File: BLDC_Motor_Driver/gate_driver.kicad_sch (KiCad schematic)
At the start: 23 parts, among them U1 TMC9660, U2 SN74LVC3G17

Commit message: added breakout connector and reformatted some things
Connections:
- net 1.8V_VOUT renamed 1V8_VOUT
- net 3.3V_REG renamed 3V3_REG
- no-connect marks 17 -> 0
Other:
- note removed: "TODO: map HALL_CONN_X to GPIOs"
- moved on the sheet: C10, C11, C12, C9, R1, R2, R3, R4, R5, R6, U2

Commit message: schematics more or less done
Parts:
- added C411, C413, C416: 100pF, Capacitor_SMD:C_0603_1608Metric, symbol Device:C
- added C418: 100nF, Capacitor_SMD:C_0603_1608Metric, symbol Device:C
- added D401: ORANGE_LED, LED_SMD:LED_0603_1608Metric, symbol Device:LED
- added R401, R402, R403: 10k, Resistor_SMD:R_0603_1608Metric, symbol Device:R_US
- added R404: 470, Resistor_SMD:R_0603_1608Metric, symbol Device:R_US
- added R405, R406, R407: 100, Resistor_SMD:R_0603_1608Metric, symbol Device:R_US
- added R411, R413, R416: 4.7k, Resistor_SMD:R_0603_1608Metric, symbol Device:R_US
- added U403: SN74LVC3G17, Package_SO:VSSOP-8_2.3x2mm_P0.5mm, symbol Buffer_Texas:SN74LVC3G17
- C401: renamed from C22; value C -> 270nF; footprint (none) -> Capacitor_SMD:C_0603_1608Metric
- C408: renamed from C19; footprint (none) -> Capacitor_SMD:C_1206_3216Metric
- renumbered C13 to C402, C14 to C403, C15 to C404, C16 to C405, C17 to C406, C18 to C407, C20 to C409, C21 to C410, C9 to C412, C10 to C414, C11 to C415, C12 to C417, L2 to L401, R1 to R408, R2 to R409, R3 to R410, R4 to R412, R5 to R414, R6 to R415, U1 to U401, U2 to U402
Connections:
- net 36V_VIN: now also R401.1, R402.1
- net 3V3_REG: now also R403.1, R404.1
- net 5V_DRV: now also C418.1, R411.1, R413.1, R416.1, U403.8 (V_{CC})
- net DRIVER_FAULTN: now also D401.1 (K), R403.2
- net DRIVER_RSTN: now also R402.2
- net DRIVER_WAKE: now also R401.2
- net GND: now also C411.2, C413.2, C416.2, C418.2, U403.4 (GND)
- net at U401.14 (DNC): no longer U401.15 (DNC)
- net DRIVER_GPIO5 renamed GPIO5
- net DRIVER_OSC_IN renamed GPIO0
- net DRIVER_OSC_OUT renamed GPIO1
- net DRIVER_TIM0_PWM renamed GPIO18
- net DRIVER_TIM_IN0 renamed GPIO15
- net DRIVER_TIM_IN1 renamed GPIO16
- net DRIVER_TIM_IN2 renamed GPIO17
- net I2C_SDA renamed ENC_N
- net ENC_N: now also U403.2 (3Y)
- net SPI0_CS1 renamed ENC_B
- net ENC_B: now also U403.5 (2Y)
- net UART_TXEN renamed ENC_A/TXEN
- net ENC_A/TXEN: now also U403.7 (1Y)
- new net: C413.1, R406.2, R413.2, U403.3 (2A)
- new net: C411.1, R407.2, R411.2, U403.6 (3A)
- new net: C416.1, R405.2, R416.2, U403.1 (1A)
- new net: D401.2 (A), R404.2
- new net ENC_A_CONN: R405.1
- new net ENC_B_CONN: R406.1
- new net ENC_N_CONN: R407.1
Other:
- note added: "Encoder"
- note removed: "TODO: do we need 4th Y phase? this HBRIDGE interface Y is meant for electric brakes... maybe pursue?"
- company: (none) -> University of Illinois Urbana-Champaign
- title: (none) -> BLDC Motor Inverter Gate Driver Circuitry
- moved on the sheet: C401, C402, C403, C404, C405, C406, C407, C408, C409, C410, C412, C414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

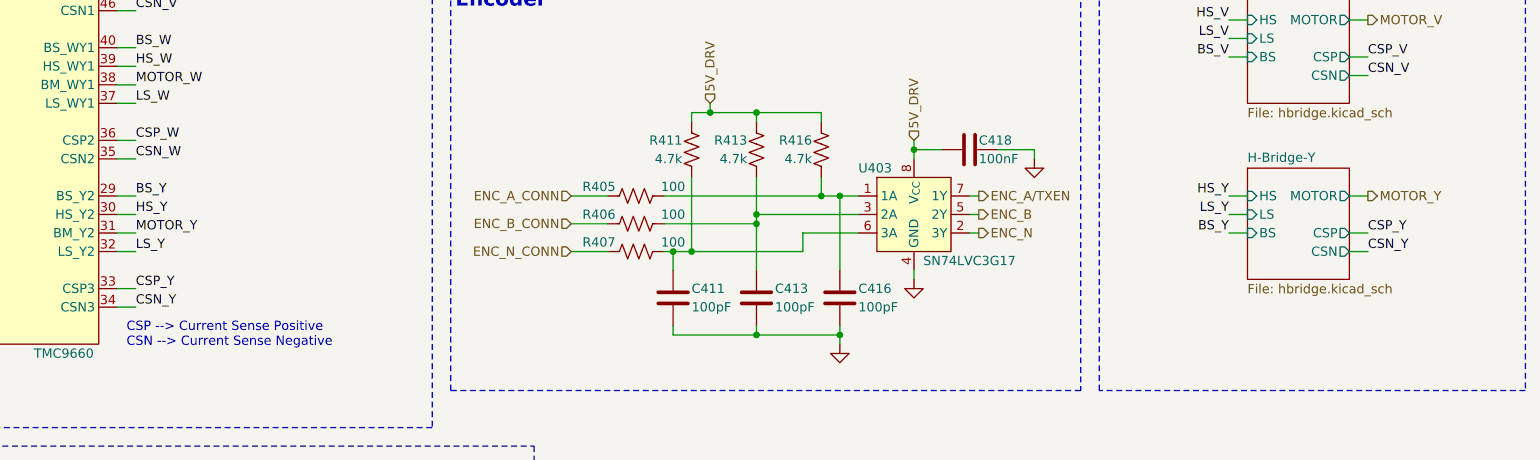
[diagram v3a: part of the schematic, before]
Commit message: removed unnecessary Y phase. finished Motor Conn Layout
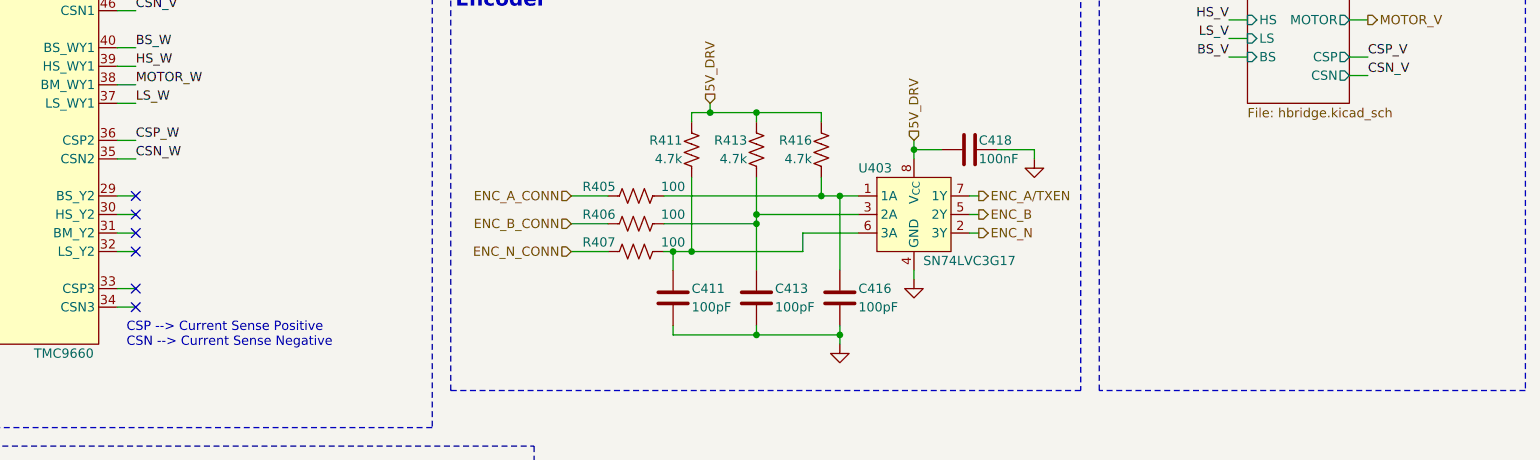
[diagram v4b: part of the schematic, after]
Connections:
- net BS_Y: no longer names the net of U401.29 (BS_Y2)
- net CSN_Y: no longer names the net of U401.34 (CSN3)
- net CSP_Y: no longer names the net of U401.33 (CSP3)
- net HS_Y: no longer names the net of U401.30 (HS_Y2)
- net LS_Y: no longer names the net of U401.32 (LS_Y2)
- net MOTOR_Y: no longer names the net of U401.31 (BM_Y2)
- no-connect marks 0 -> 6
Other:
- removed sheet H-Bridge-Y

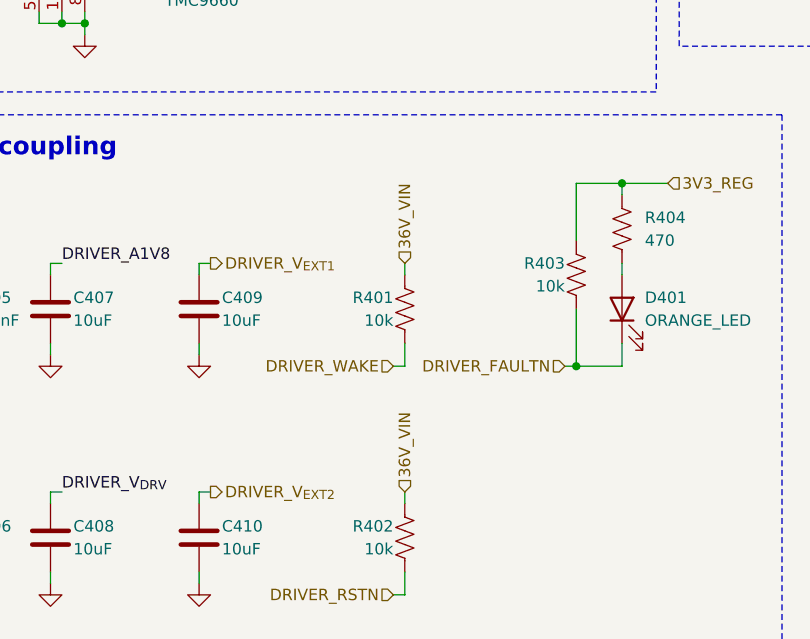
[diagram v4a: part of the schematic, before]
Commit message: changed rst/en pullups to 3V3, rerouted 5V regulator
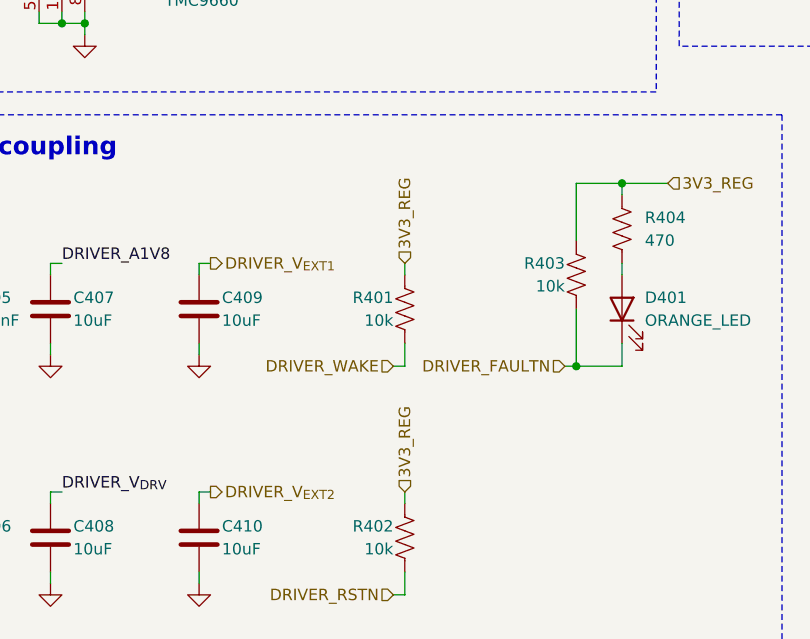
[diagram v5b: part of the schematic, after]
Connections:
- net 36V_VIN: no longer R401.1, R402.1
- net 3V3_REG: now also R401.1, R402.1
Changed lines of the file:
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@@
+		)
+	)
+	(hierarchical_label "3V3_REG"
+		(shape input)
+		(at 104.14 179.07 90)
+		(effects
+			(font
+				(size 1.27 1.27)
+			)
+			(justify left)
 		)
 	)
@@
 			)
 			(justify right)
+		)
+	)
+	(hierarchical_label "3V3_REG"
+		(shape input)
+		(at 104.14 153.67 90)
+		(effects
+			(font
+				(size 1.27 1.27)
+			)
+			(justify left)
 		)
 	)
@@
 		)
 	)
-	(hierarchical_label "36V_VIN"
-		(shape input)
-		(at 104.14 153.67 90)
-		(effects
-			(font
-				(size 1.27 1.27)
-			)
-			(justify left)
-		)
-	)
-	(hierarchical_label "36V_VIN"
-		(shape input)
-		(at 104.14 179.07 90)
-		(effects
-			(font
-				(size 1.27 1.27)
-			)
-			(justify left)
-		)
-	)
